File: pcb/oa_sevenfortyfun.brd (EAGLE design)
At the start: 88.9 x 63.4 mm, 33 parts, among them Q1 2N3904, Q10 2N3904, Q11 2N3904, Q12 2N3904, Q13 2N3904, Q14 2N3904, Q15 2N3906, Q16 2N3904, Q17 2N3906, Q18 2N3906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

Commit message: updating
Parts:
- added J1, J2, J3, J4, J5, J6, J7, J8: 1X01, Ai_Connectors:1X01
- added STANDOFF1, STANDOFF2, STANDOFF3, STANDOFF4: STAND-OFF, Ai_Electromechanical:STAND-OFF
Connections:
- removed net OFFSET1: Q6.1, R1.P$1
- removed net OFFSET2: Q7.1, R2.P$1
- new net NC: J8.1
- new net OFFSET_N1: J1.1, Q6.1, R1.P$1
- new net OFFSET_N2: J5.1, Q7.1, R2.P$1
- net IN+: now also J3.1
- net IN-: now also J2.1
- net OUT: now also J6.1
- net VCC+: now also J7.1
- net VCC-: now also J4.1
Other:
- outline, holes or cut-outs redrawn
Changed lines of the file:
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@@
 <wire x1="88.43558125" y1="63.373" x2="0.567959375" y2="63.373" width="0.2032" layer="20"/>
 <wire x1="0.567959375" y1="63.373" x2="0" y2="62.805040625" width="0.2032" layer="20" curve="90"/>
-<wire x1="0" y1="62.805040625" x2="0" y2="0.46441875" width="0.2032" layer="20"/>
+<wire x1="0" y1="62.805040625" x2="0" y2="36.195" width="0.2032" layer="20"/>
+<wire x1="0" y1="27.305" x2="0" y2="0.46441875" width="0.2032" layer="20"/>
 <wire x1="0" y1="0.46441875" x2="0.46441875" y2="0" width="0.2032" layer="20" curve="90"/>
 <wire x1="0.46441875" y1="0" x2="88.392" y2="0" width="0.2032" layer="20"/>
@@
 <text x="52.07" y="59.69" size="1.524" layer="21" font="vector" ratio="15">GAIN STAGE</text>
 <text x="69.85" y="59.69" size="1.524" layer="21" font="vector" ratio="15">OUTPUT STAGE</text>
+<wire x1="0" y1="36.195" x2="0" y2="27.305" width="0.2032" layer="20" curve="-180"/>
 </plain>
 <attributes>
@@
 <element name="R11" library="Ai_Passives" package="RES-AXIAL-0.4" value="" x="81.28" y="19.05" rot="R270"/>
 <element name="Q15" library="Ai_DiscreteSemis" package="TO-92-PNP" value="2N3906" x="81.28" y="7.62"/>
+<element name="STANDOFF1" library="Ai_Electromechanical" package="STAND-OFF" value="STAND-OFF" x="2.54" y="2.54"/>
+<element name="STANDOFF2" library="Ai_Electromechanical" package="STAND-OFF" value="STAND-OFF" x="86.36" y="2.54"/>
+<element name="STANDOFF3" library="Ai_Electromechanical" package="STAND-OFF" value="STAND-OFF" x="2.54" y="60.96"/>
+<element name="STANDOFF4" library="Ai_Electromechanical" package="STAND-OFF" value="STAND-OFF" x="86.36" y="60.96"/>
+<element name="J1" library="Ai_Connectors" package="1X01" value="1X01" x="17.78" y="2.54"/>
+<element name="J2" library="Ai_Connectors" package="1X01" value="1X01" x="35.56" y="2.54"/>
+<element name="J3" library="Ai_Connectors" package="1X01" value="1X01" x="53.34" y="2.54"/>
+<element name="J4" library="Ai_Connectors" package="1X01" value="1X01" x="71.12" y="2.54"/>
+<element name="J5" library="Ai_Connectors" package="1X01" value="1X01" x="71.12" y="60.96"/>
+<element name="J6" library="Ai_Connectors" package="1X01" value="1X01" x="53.34" y="60.96"/>
+<element name="J7" library="Ai_Connectors" package="1X01" value="1X01" x="34.29" y="60.96"/>
+<element name="J8" library="Ai_Connectors" package="1X01" value="1X01" x="17.78" y="60.96"/>
 </elements>
 <signals>
@@
 <wire x1="19.05" y1="15.24" x2="19.05" y2="30.48" width="0" layer="19" extent="1-1"/>
 </signal>
-<signal name="OFFSET2">
+<signal name="OFFSET_N2">
 <contactref element="Q7" pad="1"/>
 <contactref element="R2" pad="P$1"/>
+<contactref element="J5" pad="1"/>
 <wire x1="26.67" y1="15.24" x2="26.67" y2="20.32" width="0" layer="19" extent="1-1"/>
-</signal>
-<signal name="OFFSET1">
-<contactref element="Q6" pad="1"/>
-<contactref element="R1" pad="P$1"/>
-<wire x1="11.43" y1="15.24" x2="11.43" y2="20.32" width="0" layer="19" extent="1-1"/>
+<wire x1="71.12" y1="60.96" x2="26.67" y2="15.24" width="0" layer="19" extent="1-1"/>
 </signal>
 <signal name="N$9">
@@
 <signal name="IN+">
 <contactref element="Q2" pad="2"/>
+<contactref element="J3" pad="1"/>
+<wire x1="53.34" y1="2.54" x2="11.43" y2="48.26" width="0" layer="19" extent="1-1"/>
 </signal>
 <signal name="IN-">
 <contactref element="Q1" pad="2"/>
+<contactref element="J2" pad="1"/>
+<wire x1="35.56" y1="2.54" x2="26.67" y2="48.26" width="0" layer="19" extent="1-1"/>
 </signal>
 <signal name="N$10">
@@
 <contactref element="Q15" pad="3"/>
 <contactref element="R11" pad="P$2"/>
-<wire x1="81.28" y1="13.97" x2="81.28" y2="5.08" width="0" layer="19" extent="1-1"/>
+<contactref element="J6" pad="1"/>
+<wire x1="81.28" y1="5.08" x2="81.28" y2="13.97" width="0" layer="19" extent="1-1"/>
+<wire x1="53.34" y1="60.96" x2="81.28" y2="5.08" width="0" layer="19" extent="1-1"/>
 </signal>
 <signal name="VCC-">
@@
 <contactref element="R9" pad="P$2"/>
 <contactref element="Q15" pad="1"/>
+<contactref element="J4" pad="1"/>
 <wire x1="66.04" y1="15.24" x2="81.28" y2="10.16" width="0" layer="19" extent="1-1"/>
-<wire x1="52.07" y1="12.7" x2="66.04" y2="15.24" width="0" layer="19" extent="1-1"/>
-<wire x1="11.43" y1="5.08" x2="52.07" y2="12.7" width="0" layer="19" extent="1-1"/>
-<wire x1="19.05" y1="5.08" x2="11.43" y2="5.08" width="0" layer="19" extent="1-1"/>
-<wire x1="26.67" y1="5.08" x2="19.05" y2="5.08" width="0" layer="19" extent="1-1"/>
-<wire x1="36.83" y1="5.08" x2="26.67" y2="5.08" width="0" layer="19" extent="1-1"/>
-<wire x1="45.72" y1="26.67" x2="36.83" y2="5.08" width="0" layer="19" extent="1-1"/>
-<wire x1="58.42" y1="15.24" x2="45.72" y2="26.67" width="0" layer="19" extent="1-1"/>
+<wire x1="58.42" y1="15.24" x2="66.04" y2="15.24" width="0" layer="19" extent="1-1"/>
+<wire x1="52.07" y1="12.7" x2="58.42" y2="15.24" width="0" layer="19" extent="1-1"/>
+<wire x1="45.72" y1="26.67" x2="52.07" y2="12.7" width="0" layer="19" extent="1-1"/>
+<wire x1="36.83" y1="5.08" x2="52.07" y2="12.7" width="0" layer="19" extent="1-1"/>
+<wire x1="26.67" y1="5.08" x2="36.83" y2="5.08" width="0" layer="19" extent="1-1"/>
+<wire x1="19.05" y1="5.08" x2="26.67" y2="5.08" width="0" layer="19" extent="1-1"/>
+<wire x1="11.43" y1="5.08" x2="19.05" y2="5.08" width="0" layer="19" extent="1-1"/>
+<wire x1="71.12" y1="2.54" x2="11.43" y2="5.08" width="0" layer="19" extent="1-1"/>
 </signal>
 <signal name="VCC+">
@@
 <contactref element="Q20" pad="3"/>
 <contactref element="Q13" pad="3"/>
-<wire x1="19.05" y1="35.56" x2="81.28" y2="49.53" width="0" layer="19" extent="1-1"/>
-<wire x1="19.05" y1="52.07" x2="19.05" y2="35.56" width="0" layer="19" extent="1-1"/>
-<wire x1="36.83" y1="52.07" x2="19.05" y2="52.07" width="0" layer="19" extent="1-1"/>
-<wire x1="45.72" y1="52.07" x2="36.83" y2="52.07" width="0" layer="19" extent="1-1"/>
-<wire x1="66.04" y1="52.07" x2="45.72" y2="52.07" width="0" layer="19" extent="1-1"/>
+<contactref element="J7" pad="1"/>
+<wire x1="66.04" y1="52.07" x2="81.28" y2="49.53" width="0" layer="19" extent="1-1"/>
+<wire x1="45.72" y1="52.07" x2="66.04" y2="52.07" width="0" layer="19" extent="1-1"/>
+<wire x1="36.83" y1="52.07" x2="45.72" y2="52.07" width="0" layer="19" extent="1-1"/>
+<wire x1="19.05" y1="52.07" x2="36.83" y2="52.07" width="0" layer="19" extent="1-1"/>
+<wire x1="19.05" y1="35.56" x2="19.05" y2="52.07" width="0" layer="19" extent="1-1"/>
+<wire x1="34.29" y1="60.96" x2="19.05" y2="35.56" width="0" layer="19" extent="1-1"/>
+</signal>
+<signal name="OFFSET_N1">
+<contactref element="J1" pad="1"/>
+<contactref element="Q6" pad="1"/>
+<contactref element="R1" pad="P$1"/>
+<wire x1="11.43" y1="15.24" x2="11.43" y2="20.32" width="0" layer="19" extent="1-1"/>
+<wire x1="17.78" y1="2.54" x2="11.43" y2="15.24" width="0" layer="19" extent="1-1"/>
+</signal>
+<signal name="NC">
+<contactref element="J8" pad="1"/>
 </signal>
 </signals>

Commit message: Working on silkscreen
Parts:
- added J9: 2X04, Ai_Connectors:2X04
- J1, J2, J3, J4, J5, J6, J7, J8: value 1X01 -> 1X01-TERM; device Ai_Connectors:1X01 -> Ai_Connectors:1X01-TERM
- moved Q15 10.2 mm to (76.2, 16.5)
- moved R10 10.2 mm to (76.2, 40.6)
- moved Q8 10.0 mm to (36.8, 32.9)
- moved R11 9.69 mm to (76.2, 27.3)
- moved STANDOFF3 7.62 mm to (2.54, 68.6)
- moved STANDOFF4 7.62 mm to (86.4, 68.6)
- moved R1 7.08 mm to (14.0, 16.8)
- moved R9 6.84 mm to (63.5, 16.5)
- moved R2 6.84 mm to (29.2, 16.5)
- moved R3 6.84 mm to (21.6, 16.5)
- moved R8 6.84 mm to (55.9, 16.5)
- moved Q13 6.75 mm to (76.2, 51.4)
- moved U$3 6.59 mm to (4.70, 5.84)
- moved R4 6.35 mm to (36.8, 16.5)
- moved Q12 6.25 mm to (63.5, 27.3)
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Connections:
- net IN+: now also J9.5
- net IN-: now also J9.3
- net NC: now also J9.2
- net OFFSET_N1: now also J9.1
- net OFFSET_N2: now also J9.8
- net OUT: now also J9.6
- net VCC+: now also J9.4
- net VCC-: now also J9.7
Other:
- board size 88.9 x 63.4 mm -> 88.9 x 71.1 mm
- board text added: "1"
- board text added: "2"
- board text added: "3"
- board text added: "4"
- board text added: "5"
- board text added: "6"
- board text added: "7"
- board text added: "8"
- board text added: "BREAKOUT"
- board text added: "DIFFERENTIAL AMPLIFIER"
- board text added: "IN+"
- board text added: "IN-"
- board text added: "NC"
- board text added: "OFFSET N1"
- board text added: "OFFSET N2"
- board text added: "OUT"
- board text added: "VCC+"
- board text added: "VCC-"
- board text removed: "DIFERENTIAL AMPLIFIER"

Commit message: Working on silkscreen
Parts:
- moved Q8 10.5 mm to (38.2, 43.3)
- moved C1 6.16 mm to (51.1, 46.6)
- moved R5 3.51 mm to (45.8, 46.0)
- moved Q9 3.02 mm to (45.8, 24.8)
- moved J9 1.80 mm to (83.8, 35.6)
- moved Q11 1.55 mm to (51.1, 16.1)
- moved R4 1.42 mm to (38.2, 16.8)
- moved Q10 0.85 mm to (56.6, 26.9)
- moved Q12 0.85 mm to (64.3, 26.9)
- moved R7 0.85 mm to (56.6, 37.7)
- moved Q16 0.80 mm to (64.3, 42.2)
- moved R6 0.80 mm to (56.6, 51.1)
- moved R11 0.80 mm to (77.0, 27.6)
- moved Q13 0.80 mm to (77.0, 51.7)
- moved Q14 0.80 mm to (70.6, 35.8)
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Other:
- board text added: "741"
- board text added: "SevenFortyFun"

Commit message: starting to route
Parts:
- C1: value (none) -> 30pF
- J9: value 2X04 -> 2X04SHR; device Ai_Connectors:2X04 -> Ai_Connectors:2X04-SHR
- R1, R2: value (none) -> 1K
- R10: value (none) -> 25
- R11, R9: value (none) -> 50
- R3, R8: value (none) -> 50K
- R4: value (none) -> 5K
- R5: value (none) -> 39K
- R6: value (none) -> 4.5K
- R7: value (none) -> 7.5K
- U$3: value AI-LOGOXS -> AI-LOGOL; device Ai_Miscellany:AI-LOGO-XS -> Ai_Miscellany:AI-LOGO-L
- moved Q4 4.50 mm to (12.7, 36.8)
- moved U$3 4.26 mm to (6.60, 9.65)
- moved R5 3.43 mm to (45.7, 42.5)
- moved Q5 3.42 mm to (20.3, 32.4)
- moved Q2 2.62 mm to (12.7, 47.0)
- moved Q16 2.34 mm to (64.8, 44.5)
- moved R1 1.71 mm to (12.7, 15.9)
- moved Q1 1.55 mm to (27.9, 47.6)
- moved R2 1.55 mm to (27.9, 15.9)
- moved R3 1.55 mm to (20.3, 15.9)
- moved Q6 1.42 mm to (12.7, 26.4)
- moved Q7 1.42 mm to (27.9, 27.1)
- moved C1 1.35 mm to (52.1, 45.7)
- moved Q3 1.33 mm to (27.9, 37.0)
- moved Q17 1.30 mm to (20.3, 53.3)
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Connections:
- removed net N$23: Q12.3, Q16.1
- removed net N$25: Q14.1, R10.P$2, R11.P$1
- new net N$7: Q15.3, R11.P$2
- net N$18: now also Q12.3, Q15.2, Q16.1
- net OUT: now also Q14.1, R10.P$2, R11.P$1; no longer Q15.3, R11.P$2
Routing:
- net VCC-: track 0.00 -> 24.8 mm
- net OFFSET_N1: track 0.00 -> 20.3 mm
- net VCC+: track 0.00 -> 15.9 mm
- net N$16: track 0.00 -> 12.7 mm
- net N$6: track 0.00 -> 8.89 mm
- net OFFSET_N2: track 0.00 -> 3.56 mm
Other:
- outline, holes or cut-outs redrawn
- board text removed: "CO"
- board text removed: "v1.0"

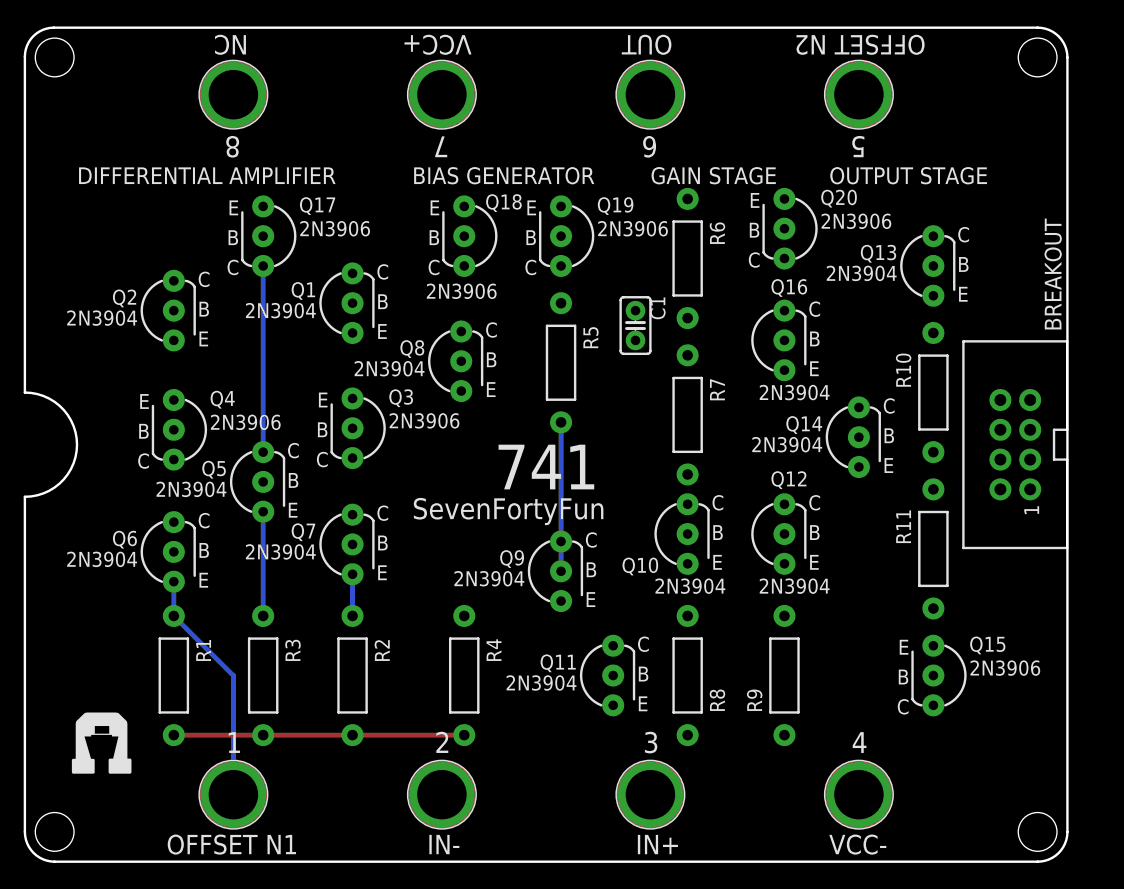
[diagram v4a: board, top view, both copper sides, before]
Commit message: Routed. Worked on silkscreen.
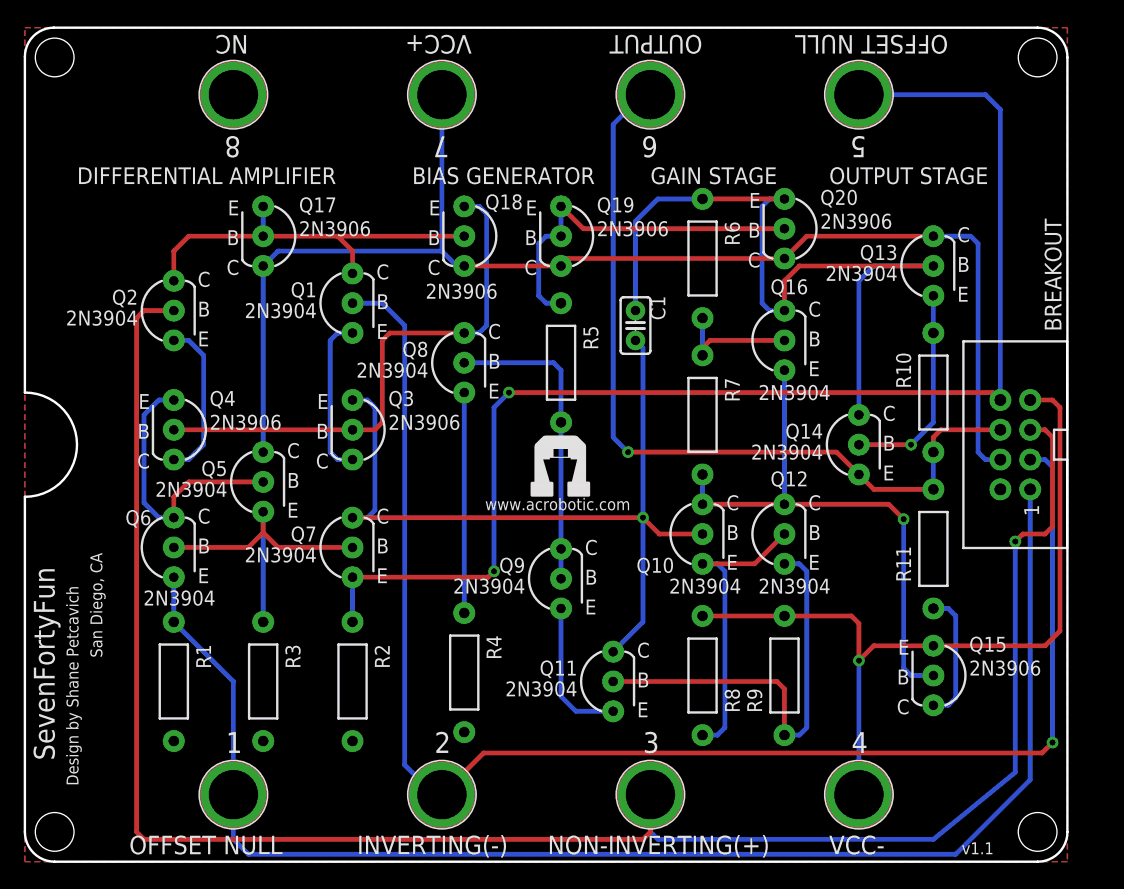
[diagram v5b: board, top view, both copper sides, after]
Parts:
- moved U$3 45.7 mm to (45.7, 33.3)
- moved Q10 1.27 mm to (57.8, 27.9)
- moved R6 1.27 mm to (57.8, 51.4)
- moved R7 1.27 mm to (57.8, 38.1)
- moved R8 1.27 mm to (57.8, 15.9)
- moved Q9 0.64 mm to (45.7, 24.1)
- moved Q14 0.63 mm to (71.1, 35.6)
- moved Q11 0.51 mm to (50.2, 15.4)
- moved R1 0.51 mm to (12.7, 15.4)
- moved R2 0.51 mm to (27.9, 15.4)
- moved R3 0.51 mm to (20.3, 15.4)
- moved Q6 0.38 mm to (12.7, 26.8)
- moved Q8 0.28 mm to (37.5, 42.5)
- moved R4 0.25 mm to (37.5, 16.1)
- moved Q7 0.25 mm to (27.9, 26.8)
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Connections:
- removed net NC: J8.1, J9.2
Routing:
- net IN+: track 0.00 -> 164.5 mm, vias 0 -> 1
- net IN-: track 0.00 -> 126.5 mm, vias 0 -> 1
- net OFFSET_N2: track 3.56 -> 111.4 mm, vias 0 -> 2
- net OFFSET_N1: track 20.3 -> 120.3 mm
- net VCC+: track 15.9 -> 112.5 mm
- net N$5: track 0.00 -> 71.4 mm, vias 0 -> 1
- net OUT: track 0.00 -> 70.5 mm, vias 0 -> 1
- net N$22: track 0.00 -> 67.8 mm
- net VCC-: track 24.8 -> 80.7 mm, vias 0 -> 1
- net N$18: track 0.00 -> 47.1 mm, vias 0 -> 1
- net N$9: track 0.00 -> 46.1 mm
- net N$21: track 0.00 -> 36.5 mm
- net N$1: track 0.00 -> 34.1 mm
- net N$15: track 0.00 -> 31.8 mm
- net N$14: track 0.00 -> 25.7 mm
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- added copper zone on layer 1, net VCC-
- added copper zone on layer 16, net VCC-
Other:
- board text added: "Design by Shane Petcavich"
- board text added: "INVERTING(-)"
- board text added: "NON-INVERTING(+)"
- board text added: "OFFSET NULL"
- board text added: "OUTPUT"
- board text added: "San Diego, CA"
- board text added: "v1.1"
- board text added: "www.acrobotic.com"
- board text removed: "741"
- board text removed: "IN+"
- board text removed: "IN-"
- board text removed: "OFFSET N1"
- board text removed: "OFFSET N2"
- board text removed: "OUT"
